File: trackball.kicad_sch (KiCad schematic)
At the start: 196 parts, among them J1 ZX-PM2.0-2-4PY, Q1 SI2302_C2891732, SW1 HX TC-5608-Y, SW2 HX TC-5608-Y, SW3 HX TC-5608-Y, SW4 HX TC-5608-Y, SW5 HX TC-5608-Y, SW6 HX TC-5608-Y, SW7 HX TC-5608-Y, SW8 HX TC-5608-Y, U1 SY8089A1AAC, U10 WS2812B, U11 WS2812B, U12 WS2812B, U13 WS2812B, U14 WS2812B, U15 WS2812B, U16 WS2812B, U17 WS2812B, U18 WS2812B, U19 WS2812B, U2 USB-TYPE-C-017, U20 WS2812B, U21 ANT3216LL00R2400A, U3 PMW3610, U4 PMW3610, U5 WS2812B, U6 WS2812B, U7 WS2812B, U8 WS2812B, U9 WS2812B, X1 XL7EL89CKI-111YLC-32M

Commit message: chore: checkpoint
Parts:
- added R67: FRC0402F1002TS, easyeda2kicad:R0402, symbol easyeda2kicad:FRC0402F1002TS
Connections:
- net 3V3: now also R56.2, R67.1
- net CHG_ISACTIVE: now also LED6.1 (K); no longer R56.2
- net GND: no longer LED6.1 (K)
- net at LED6.2 (A), R56.1: now also R67.2
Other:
- moved on the sheet: LED1, LED2, LED3, LED4, LED5, LED6, R44, R46, R47, R49, R50, R51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

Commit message: chore: checkpoint
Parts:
- added R68: HPCR0402F160KK9, easyeda2kicad:R0402, symbol easyeda2kicad:HPCR0402F160KK9
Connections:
- net 3V3: now also R68.2
- net at Q1.1 (G), R57.2: now also R68.1
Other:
- moved on the sheet: C2, D1, LED10, LED11, LED12, LED13, LED14, LED15, LED7, LED8, LED9, R11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

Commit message: feat: rev.02 hardware
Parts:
- removed BAT1: ZX-SH1.0-3PLT, easyeda2kicad:CONN-SMD_3P-P1.00_HDGC_HDGC1002WV-S-3P, symbol easyeda2kicad:ZX-SH1.0-3PLT
- removed C1: CL05A106MP5NUNC_C315248, easyeda2kicad:C0402, symbol easyeda2kicad:CL05A106MP5NUNC_C315248
- removed C13, C14, C15, C17, C18, C19, C20, C24, C25, C28, C32, C33, C37, C38, C42, C46, C48, C49, C54, C55, C57: TCC0402X7R103M500AT, easyeda2kicad:C0402, symbol easyeda2kicad:TCC0402X7R103M500AT
- removed C16, C21, C22, C23, C30, C36, C43, C45, C51, C52: CC0402KRX7R7BB104, easyeda2kicad:C0402, symbol easyeda2kicad:CC0402KRX7R7BB104
- removed C2, C26, C27, C29, C4, C5, C56, C58, C59, C8: CL05A105KP5NNNC, easyeda2kicad:C0402, symbol easyeda2kicad:CL05A105KP5NNNC
- removed C3, C40, C41: CC0402FRNPO9BN120, easyeda2kicad:C0402, symbol easyeda2kicad:CC0402FRNPO9BN120
- removed C35: 0402CG1R0C500NT, easyeda2kicad:C0402, symbol easyeda2kicad:0402CG1R0C500NT
- removed C39: 0402CG1R2C500NT, easyeda2kicad:C0402, symbol easyeda2kicad:0402CG1R2C500NT
- removed C44, C50: 0402CG821J500NT, easyeda2kicad:C0402, symbol easyeda2kicad:0402CG821J500NT
- removed L1, L2: MDA4020-1R0M, easyeda2kicad:IND-SMD_L4.5-W4.1_GSSM0420, symbol easyeda2kicad:MDA4020-1R0M
- removed LED1, LED2, LED3, LED4, LED5: XL-1005UGC, easyeda2kicad:LED0402-RD_GREEN, symbol easyeda2kicad:XL-1005UGC
- removed LED15: PD15-22C/TR8, easyeda2kicad:SENSOR-SMD_PD15-22C-TR8, symbol easyeda2kicad:PD15-22C_TR8
- removed Q1: SI2302_C2891732, easyeda2kicad:SOT-23-3_L2.9-W1.3-P1.90-LS2.4-BR, symbol easyeda2kicad:SI2302_C2891732
- removed R1, R10, R15, R16, R20, R21, R22, R23, R24, R27, R28, R3, R32, R33, R34, R37, R38, R39, R4, R40, R41, R42, R45, R48, R54, R55, R68, R9: HPCR0402F160KK9, easyeda2kicad:R0402, symbol easyeda2kicad:HPCR0402F160KK9
- removed R11, R12, R13, R14, R17, R18, R19, R2, R25, R26, R29, R30, R31, R35, R36, R43, R44, R46, R47, R49, R50, R51, R56, R57, R6, R65, R66, R67, R7, R8: FRC0402F1002TS, easyeda2kicad:R0402, symbol easyeda2kicad:FRC0402F1002TS
- removed R52, R53: FRC0402P000 TS, easyeda2kicad:R0402, symbol easyeda2kicad:FRC0402P000TS
- removed SW_RST1: TS24CA, easyeda2kicad:SW-SMD_TS24CA, symbol easyeda2kicad:TS24CA
- removed U1: SY8089A1AAC, easyeda2kicad:TSOT-23-5_L2.9-W1.6-P0.95-LS2.8-BR, symbol easyeda2kicad:SY8089A1AAC
- removed U21: ANT3216LL00R2400A, easyeda2kicad:ANT-SMD_L3.2-W1.6, symbol easyeda2kicad:ANT3216LL00R2400A
- added BAT1: HCZZ0032-3, easyeda2kicad:CONN-SMD_HCZZ0032-3, symbol easyeda2kicad:HCZZ0032-3
- added C1, C14, C15, C2, C3, C51, C52, C53, C59, C62, C64, C65, C7, C72, C9: CGA0201X5R105M6R3ET, easyeda2kicad:C0201, symbol easyeda2kicad:CGA0201X5R105M6R3ET
- added C12, C16, C19, C20, C26, C27, C28, C29, C30, C31, C32, C33, C35, C39, C40, C41, C42, C43, C44, C61, C67: 0201B103K160NT, easyeda2kicad:C0201, symbol easyeda2kicad:0201B103K160NT
- added C17: GRM155R60J226ME11D, easyeda2kicad:C0402, symbol easyeda2kicad:GRM155R60J226ME11D
- added C18: CL05A106MP5NUNC_C315248, easyeda2kicad:C0402, symbol easyeda2kicad:CL05A106MP5NUNC_C315248
- added C21, C45: 0201CG120J500NT, easyeda2kicad:C0201, symbol easyeda2kicad:0201CG120J500NT
- added C22, C24, C34, C37, C47, C48, C49, C50, C54, C58: CGA0201X5R104K100ET, easyeda2kicad:C0201, symbol easyeda2kicad:CGA0201X5R104K100ET
- added C46: 0201CG1R0C250NT, easyeda2kicad:C0201, symbol easyeda2kicad:0201CG1R0C250NT
- added C57: CGA0201C0G1R2C500ET, easyeda2kicad:C0201, symbol easyeda2kicad:CGA0201C0G1R2C500ET
- added C6, C71: (no value), easyeda2kicad:C0201, symbol easyeda2kicad:CC0201KRX7R7BB151
- added C60, C63, C66: 0201B821K500NT, easyeda2kicad:C0201, symbol easyeda2kicad:0201B821K500NT
- added J1: Conn_01x02, symbol Connector_Generic:Conn_01x02
- added L1, L3: FTC252012SR47MBCA, easyeda2kicad:IND-SMD_L2.5-W2.0, symbol easyeda2kicad:FTC252012SR47MBCA
- added L2: FTC252012S1R0MBCD, easyeda2kicad:L1008, symbol easyeda2kicad:FTC252012S1R0MBCD
- added LED10, LED8: TZ-P2-0402RTIA1-0.45T, easyeda2kicad:LED0402-RD_RED, symbol easyeda2kicad:TZ-P2-0402RTIA1-0.45T
- added Q1, Q2, Q4: XR2302, easyeda2kicad:SOT-23-3_L2.9-W1.3-P0.95-LS2.4-BR, symbol easyeda2kicad:XR2302
- added R1, R10, R12, R13, R14, R15, R19, R20, R21, R29, R3, R30, R33, R34, R35, R39, R40, R43, R44, R45, R46, R47, R48, R50, R51, R52, R59, R6, R65: RC-01W103JT, easyeda2kicad:R0201, symbol easyeda2kicad:RC-01W103JT
- added R11, R16, R17, R18, R2, R22, R23, R24, R25, R26, R27, R28, R31, R32, R36, R37, R38, R41, R42, R5, R7, R8: 0201WMF1603TEE, easyeda2kicad:R0201, symbol easyeda2kicad:0201WMF1603TEE
- added R61, R63, R9: RT0402BRE0750RL, easyeda2kicad:R0402, symbol easyeda2kicad:RT0402BRE0750RL
- added SW9: TS-1010-C-A, easyeda2kicad:KEY-SMD_TX-1010-X-X, symbol easyeda2kicad:TS-1010-C-A
- added U2, U3: SY80004DQD, easyeda2kicad:VSON-6_L1.5-W1.5-P0.50-TL, symbol easyeda2kicad:SY80004DQD
- renumbered C12 to C13, C60 to C23, C47 to C25, C61 to C36, C53 to C38, C7 to C4, C6 to C5, C31 to C55, C34 to C56, C9 to C8, J1 to J2, L3 to L4, L4 to L5, LED11 to LED1, LED9 to LED11, LED8 to LED12, LED7 to LED13, LED12 to LED3, LED13 to LED4, LED6 to LED5, LED14 to LED7, LED10 to LED9, R5 to R4, R61 to R49, R62 to R53, R63 to R55, R64 to R60, R60 to R62, R59 to R64, R58 to R66, R71 to R68, U2 to U1, U9 to U10, U10 to U11, U11 to U12, U12 to U13, U13 to U14, U14 to U15, U15 to U16, U16 to U17, U17 to U18, U18 to U19, U19 to U20, U20 to U21, U3 to U4, U4 to U5, U5 to U6, U6 to U7, U7 to U8, U8 to U9
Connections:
- net 1V8: now also C2.1, C47.2, C48.2, C49.2, C50.1, C51.1, C58.2, C59.1, C6.2, C62.1, C65.1, L1.2, R10.2, R12.1, R13.2, R14.2, R16.2, R17.2, R26.2, R27.2, R31.2, R32.2, R37.2, R38.2
- net 3V3: now also C14.1, C17.1, C64.2, C71.2, C72.2, J1.2 (Pin_2), L3.2, R3.2, R52.1; no longer U_CHG1.2 (LDO)
- net ADC_BAT: now also C61.2, R50.2, R51.1
- net ADC_VBUS: now also C67.2, R18.2, R24.1
- net BAT_TS: now also BAT1.2, R47.1
- net BAT_VCC: now also BAT1.1, C7.1, R51.2
- net BCKLT_GND: now also Q4.3 (D)
- net CHG_IRQ: now also R14.1
- net CHG_ISACTIVE: no longer U_MCU1.B15 (P1.03)
- net CHG_SCL: now also R12.2
- net CHG_SDA: now also R13.1
- net D_RE1_1V8: now also R22.1, R25.2, R42.2
- net D_RE1_A: now also C44.1, R42.1
- net D_RE1_B: now also C30.2, R25.1
- net D_RE1_GND: now also C16.1, C30.1, C44.2
- net D_RE1_SW: now also C16.2, R21.1
- net D_RE2_1V8: now also R28.2, R36.1, R41.2
- net D_RE2_A: now also C43.1, R41.1
- net D_RE2_B: now also C35.2, R28.1
- net D_RE2_GND: now also C31.1, C35.1, C43.2
- net D_RE2_SW: now also C31.2, R35.1
- net D_SS1_1V8: now also C37.2, R43.2
- net D_SS1_GND: now also C37.1, C39.1, C40.1
- net D_SS1_RST: now also R43.1
- net D_SS2_1V8: now also C34.2, R44.2
- net D_SS2_GND: now also C26.1, C27.1, C34.1
- net D_SS2_RST: now also R44.1
- net GND: now also BAT1.3, BAT1.4, BAT1.5, C1.2, C12.1, C14.2, C15.2, C17.2, C18.2, C19.2, C2.2, C20.2, C21.2, C28.2, C29.2, C3.2, C32.2, C33.2, C41.2, C42.2, C45.2, C46.2, C47.1, C48.1, C49.1, C50.2, C51.2, C52.1, C53.1, C54.1, C57.1, C58.1, C59.2, C60.2, C61.1, C62.2, C63.2, C64.1, C65.2, C66.1, C67.1, C72.1, C9.2, LED10.1 (K), LED8.1 (K), Q1.2 (S), Q2.2 (S), Q4.2 (S), R11.1, R18.1, R2.1, R23.1, R45.1, R46.1, R48.1, R5.1, R50.1, R7.1, SW9.1, U2.4 (GND), U3.4 (GND); no longer U10.3 (GND), U11.3 (GND), U12.3 (GND), U13.3 (GND), U14.3 (GND), U15.3 (GND), U16.3 (GND), U17.3 (GND), U18.3 (GND), U19.3 (GND), U20.3 (GND), U21.3 (GND), U6.3 (GND), U7.3 (GND), U8.3 (GND), U9.3 (GND)
- net GNDS: now also C12.2, C9.1, R8.2
- net MCU_BCKLT_EN: now also Q4.1 (G), R46.2
- net MCU_DEC46: now also C52.2
- net MCU_LED1: now also R63.2
- net MCU_LED2: now also R61.2
- net MCU_RESET: now also C66.2, R9.2
- net MCU_XC1: now also C45.1
- net MCU_XC2: now also C21.1
- net SJ_NOTS1: now also R47.2
- net SW1: now also C20.1, R19.2
- net SW2: now also C19.1, R20.2
- net SW3: now also C28.1, R30.2
- net SW4: now also C29.1, R29.2
- net SW5: now also C41.1, R33.2
- net SW6: now also C32.1, R34.2
- net SW7: now also C42.1, R40.2
- net SW8: now also C33.1, R39.2
- net USB_MUX_SEL: now also R11.2
- net USB_VBUS: now also J2.8, C1.1, C53.2, R24.2
- net VSYS: now also C15.1, C18.1, C3.1, L2.2, R1.1, R15.2, R59.1, R65.2, U2.6 (IN), U3.6 (IN)
- net at SW7.1: now also R17.1, R40.1
- net at L4.1, L5.2: now also C57.2
- net at U_MCU1.C1 (DEC1): now also C54.2
- net at U5.1 (+VCSEL), U5.10 (PASS_T): now also C27.2
- net at SW5.1: now also R26.1, R33.1
- net at SW4.1: now also R29.1, R31.1
- net at C38.2, U5.9 (VCP): now also C26.2
- net at SW1.1: now also R19.1, R37.1
- net at U4.1 (+VCSEL), U4.10 (PASS_T): now also C40.2
- net at U4.12 (CP): now also C22.2
- net at U4.13 (CN): now also C22.1
- net at C25.2, U4.9 (VCP): now also C39.2
- net at C11.2, R4.2, U_CHG1.10 (BAT)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: now also C7.2
- net at U_MCU1.D23 (DEC3): now also C60.1
- net at SW3.1: now also R30.1, R32.1
- net at U5.12 (CP): now also C24.2
- net at U5.13 (CN): now also C24.1
- net at SW8.1: now also R16.1, R39.1
- net at U_MUX1.8 (~{OE}): now also R2.2
- net at SW2.1: now also R20.1, R38.1
- net at U_RE2.E: now also R35.2, R36.2
- net at U_RE1.E: now also R21.2, R22.2
- net at L5.1, U_MCU1.H23 (ANT): now also C46.1
- net at U_MCU1.N24 (DEC5): now also C63.1
- net at LED5.2 (A): now also R52.2
- net at SW6.1: now also R27.1, R34.1
- net at U_CHG1.15 (SW), U_CHG1.16 (SW), U_CHG1.17 (SW)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: now also L2.1
- net CHG_ADC: no longer names the net of U_CHG1.6 (GPADC)
- net MCU_LED3 renamed MCU_VIB_EN
- net MCU_VIB_EN: now also Q2.1 (G), R48.2
- new net: R7.2, R8.1
- new net: R1.2, U3.1 (EN)
- new net: R15.1, U3.2 (PG)
- new net: R9.1, SW9.2
- new net: C6.1, R10.1, R5.2, U2.3 (FB)
- new net: R3.1, R6.2
- new net: LED10.2 (A), R63.1
- new net: R59.2, U2.1 (EN)
- new net: C71.1, R23.2, R6.1, U3.3 (FB)
- new net: R65.1, U2.2 (PG)
- new net: L1.1, U2.5 (LX)
- new net: LED8.2 (A), R61.1
- new net: L3.1, U3.5 (LX)
- new net MCU_RGB_EN: Q1.1 (G), R45.2, U_MCU1.B15 (P1.03)
- new net RGB_GND: Q1.3 (D), U10.3 (GND), U11.3 (GND), U12.3 (GND), U13.3 (GND), U14.3 (GND), U15.3 (GND), U16.3 (GND), U17.3 (GND), U18.3 (GND), U19.3 (GND), U20.3 (GND), U21.3 (GND), U6.3 (GND), U7.3 (GND), U8.3 (GND), U9.3 (GND)
- new net VIB_GND: J1.1 (Pin_1), Q2.3 (D)
- no-connect marks 54 -> 51
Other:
- note added: "3.3V"
- note added: "actually 3.15V"
- note added: "actually ~1.875V for LEDs stability and to ensure no need in voltage level converter"
- note removed: "alternative antenna? 5dBi stated"
- note removed: "in case if mux isn't populated"
- note removed: "programming/debug port"
- moved on the sheet: AE1, C10, C11, C13, C23, C25, C36, C38, C4, C5, C55, C56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

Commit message: chore: refactoring
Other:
- note added: "actually 1.875V for LEDs and to ensure no need in voltage level converter"
- note added: "actually 3.15V should be still in CC range for RGB LEDs"
- note removed: "actually 3.15V"
- note removed: "actually ~1.875V for LEDs stability and to ensure no need in voltage level converter"
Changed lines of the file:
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@@
 		)
 	)
-	(text "actually 3.15V"
+	(text "actually 3.15V\nshould be still in CC range for RGB LEDs"
 		(exclude_from_sim no)
-		(at 475.742 193.802 0)
+		(at 468.63 193.294 0)
 		(effects
 			(font
@@
 				(color 168 168 168 1)
 			)
+			(justify left)
 		)
 	)
-	(text "actually ~1.875V \nfor LEDs stability and to ensure no need in voltage level converter"
+	(text "actually 1.875V \nfor LEDs and to ensure no need in voltage level converter"
 		(exclude_from_sim no)
 		(at 468.376 99.568 0)

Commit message: chore: refactoring
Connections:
- net GND: now also J2.3
- net MCU_SWO: no longer names the net of U_MCU1.AD22 (P1.00/TRACEDATA0)
- net MCU_SWO: no longer J2.3
- no-connect marks 51 -> 52
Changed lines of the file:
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@@
 	(text "actually 3.15V\nshould be still in CC range for RGB LEDs"
 		(exclude_from_sim no)
-		(at 468.63 193.294 0)
+		(at 468.63 192.786 0)
 		(effects
 			(font
@@
 	)
 	(junction
+		(at 312.928 343.154)
+		(diameter 0)
+		(color 0 0 0 0)
+	)
+	(junction
 		(at 475.488 40.894)
 		(diameter 0)
@@
 	)
 	(no_connect
+		(at 518.414 321.564)
+	)
+	(no_connect
 		(at 386.334 231.648)
 	)
@@
 	(wire
 		(pts
+			(xy 312.928 338.074) (xy 312.928 343.154)
+		)
+		(stroke
+			(width 0)
+			(type default)
+		)
+	)
+	(wire
+		(pts
 			(xy 221.488 165.1) (xy 221.488 171.45)
 		)
@@
 	(wire
 		(pts
-			(xy 325.882 343.154) (xy 328.422 343.154)
+			(xy 312.928 343.154) (xy 328.422 343.154)
 		)
 		(stroke
@@
 	(wire
 		(pts
+			(xy 312.928 338.074) (xy 328.422 338.074)
+		)
+		(stroke
+			(width 0)
+			(type default)
+		)
+	)
+	(wire
+		(pts
 			(xy 390.144 259.588) (xy 390.144 260.858)
 		)
@@
 	(wire
 		(pts
-			(xy 325.882 343.154) (xy 325.882 345.694)
+			(xy 312.928 343.154) (xy 312.928 350.266)
 		)
 		(stroke
@@
 		)
 	)
-	(global_label "MCU_SWO"
-		(shape bidirectional)
-		(at 328.422 338.074 180)
-		(fields_autoplaced yes)
-		(effects
-			(font
-				(size 1.27 1.27)
-			)
-			(justify right)
-		)
-		(property "Intersheetrefs" "${INTERSHEET_REFS}"
-			(at 315.3146 338.074 0)
-			(effects
-				(font
-					(size 1.27 1.27)
-				)
-				(justify right)
-				(hide yes)
-			)
-		)
-	)
 	(global_label "D_SS2_GND"
 		(shape bidirectional)
@@
 		)
 	)
-	(global_label "MCU_SWO"
-		(shape bidirectional)
-		(at 518.414 321.564 0)
-		(fields_autoplaced yes)
-		(effects
-			(font
-				(size 1.27 1.27)
-			)
-			(justify left)
-		)
-		(property "Intersheetrefs" "${INTERSHEET_REFS}"
-			(at 531.5214 321.564 0)
-			(effects
-				(font
-					(size 1.27 1.27)
-				)
-				(justify left)
-				(hide yes)
-			)
-		)
-	)
 	(global_label "SW5"
 		(shape bidirectional)
@@
 	(symbol
 		(lib_id "power:GND")
-		(at 325.882 345.694 0)
+		(at 312.928 350.266 0)
 		(unit 1)
 		(exclude_from_sim no)
@@
 		(dnp no)
 		(property "Reference" "#PWR044"
-			(at 325.882 352.044 0)
+			(at 312.928 356.616 0)
 			(effects
 				(font
@@
 		)
 		(property "Value" "GND"
-			(at 325.882 350.012 0)
+			(at 312.928 354.584 0)
 			(effects
 				(font
@@
 		)
 		(property "Footprint" ""
-			(at 325.882 345.694 0)
+			(at 312.928 350.266 0)
 			(effects
 				(font
@@
 		)
 		(property "Datasheet" ""
-			(at 325.882 345.694 0)
+			(at 312.928 350.266 0)
 			(effects
 				(font
@@
 		)
 		(property "Description" "Power symbol creates a global label with name \"GND\" , ground"
-			(at 325.882 345.694 0)
+			(at 312.928 350.266 0)
 			(effects
 				(font

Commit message: feat: rev.03 hardware
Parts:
- removed C30, C35, C43, C44: 0201B103K160NT, easyeda2kicad:C0201, symbol easyeda2kicad:0201B103K160NT
- removed R1, R59: RC-01W103JT, easyeda2kicad:R0201, symbol easyeda2kicad:RC-01W103JT
- removed R7, R8: 0201WMF1603TEE, easyeda2kicad:R0201, symbol easyeda2kicad:0201WMF1603TEE
- added R1: 0201WMF1603TEE, easyeda2kicad:R0201, symbol easyeda2kicad:0201WMF1603TEE
- added R54, R7, R8: RC-01W103JT, easyeda2kicad:R0201, symbol easyeda2kicad:RC-01W103JT
- C6, C71: value (none) -> ~
- R10, R15, R3, R43, R44, R50, R51, R6, R65: LCSC Part C304504 -> C320848
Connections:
- net GND: now also R1.1, R7.1
- net GNDS: now also R8.2
- net MCU_RGB_EN: now also R48.2; no longer R45.2
- net MCU_VIB_EN: now also R45.2; no longer R48.2
- net VSYS: now also R54.2
- net 3V3_EN: now reaches U3.1 (EN)
- net 3V3_EN: now also U_MCU1.AD22 (P1.00/TRACEDATA0), R1.2
- net at U2.1 (EN): now also R54.1
- new net: R7.2, R8.1
- no-connect marks 52 -> 51
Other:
- note added: "actually 1.875V to ensure no need in voltage level converter and for red LEDs"
- note added: "actually 3.15V: should be still in CC range for RGB LEDs this whole power rail might be not populated if backlight and RGB aren't required"
- note removed: "actually 1.875V for LEDs and to ensure no need in voltage level converter"
- note removed: "actually 3.15V should be still in CC range for RGB LEDs"
- moved on the sheet: C14, C15, C17, C18, C59, C62, C65, C71, L3, R15, R23, R3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

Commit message: feat: wakeup source
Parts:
- removed C67: 0201B103K160NT, easyeda2kicad:C0201, symbol easyeda2kicad:0201B103K160NT
- removed R18, R24: 0201WMF1603TEE, easyeda2kicad:R0201, symbol easyeda2kicad:0201WMF1603TEE
- added C30: 0201B103K160NT, easyeda2kicad:C0201, symbol easyeda2kicad:0201B103K160NT
- added D2, D3, D4, D5, D6, D7: BAS40-06T-7-F, easyeda2kicad:SC-75-3_L1.6-W0.8-P1.00-LS1.6-BR, symbol easyeda2kicad:BAS40-06T-7-F
- added R56: RT0402BRE0750RL, easyeda2kicad:R0402, symbol easyeda2kicad:RT0402BRE0750RL
- added R57: RC-01W103JT, easyeda2kicad:R0201, symbol easyeda2kicad:RC-01W103JT
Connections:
- net 3V3: now also R57.2
- net GND: now also C30.2
- net RE1_A: now also D7.2
- net RE2_A: now also D7.1
- net SS1_MTN: now also D6.2
- net SS2_MTN: now also D6.1
- net SW1: now also D2.2
- net SW2: now also D2.1
- net SW3: now also D3.2
- net SW4: now also D3.1
- net SW5: now also D4.2
- net SW6: now also D4.1
- net SW7: now also D5.2
- net SW8: now also D5.1
- net ADC_VBUS renamed MCU_WAKEUP
- net MCU_WAKEUP: now also C30.1, R56.1, R57.1
- new net: D2.3, D3.3, D4.3, D5.3, D6.3, D7.3, R56.2
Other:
- moved on the sheet: C61, R50, R51

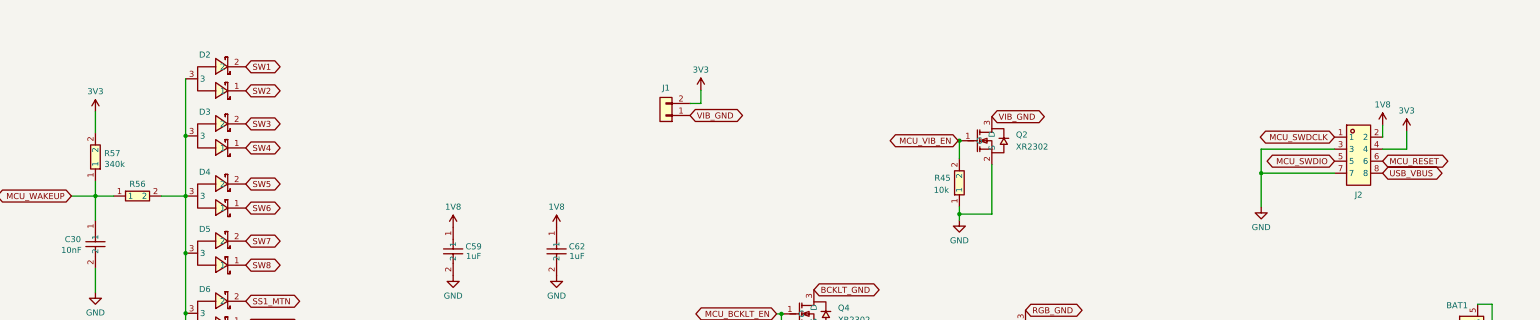
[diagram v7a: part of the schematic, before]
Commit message: bugfix: wakeup source 3V3 → 1V8 pullup
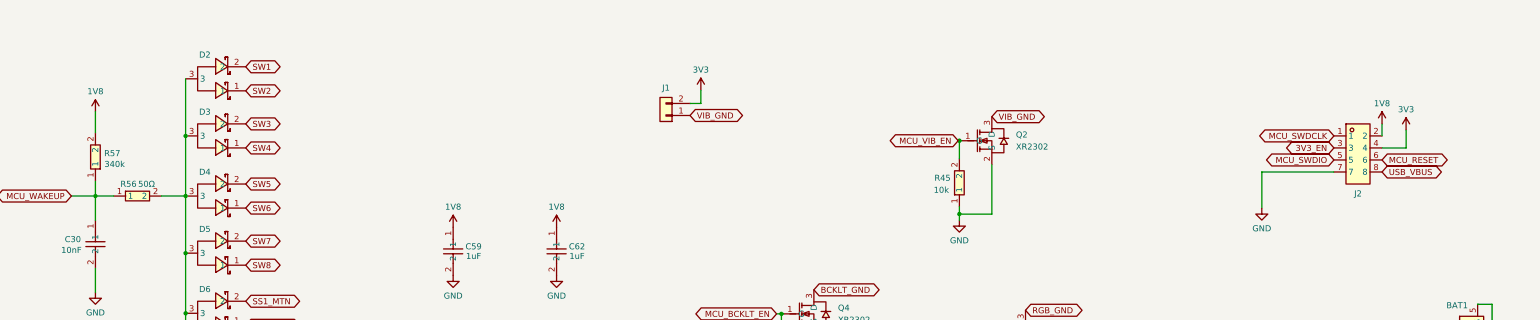
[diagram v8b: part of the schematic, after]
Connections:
- net 1V8: now also R57.2
- net 3V3: no longer R57.2
- net 3V3_EN: now also J2.3
- net GND: no longer J2.3
